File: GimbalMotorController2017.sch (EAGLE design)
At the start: 123 parts, among them J3 APP_2POS_CONFIG5V_HORIZ, Q7 MOSFET-PCHANNEL, Q8 MOSFET-PCHANNEL, Q9 MOSFET-NCHANNELAO3404A, U1 NUP4201MR6, U2 MAX3232D, U3 CSD18533Q5A, U4 CSD18533Q5A, U5 CSD18533Q5A, U6 CSD18533Q5A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

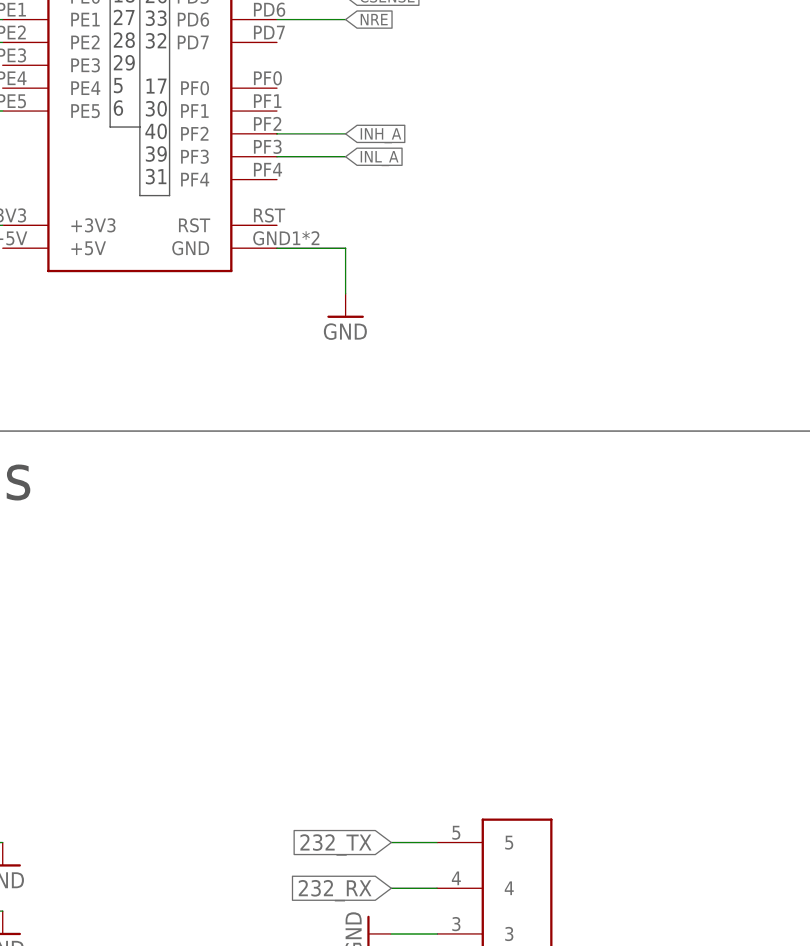
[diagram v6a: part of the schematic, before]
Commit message: Add pwm connector to external connections
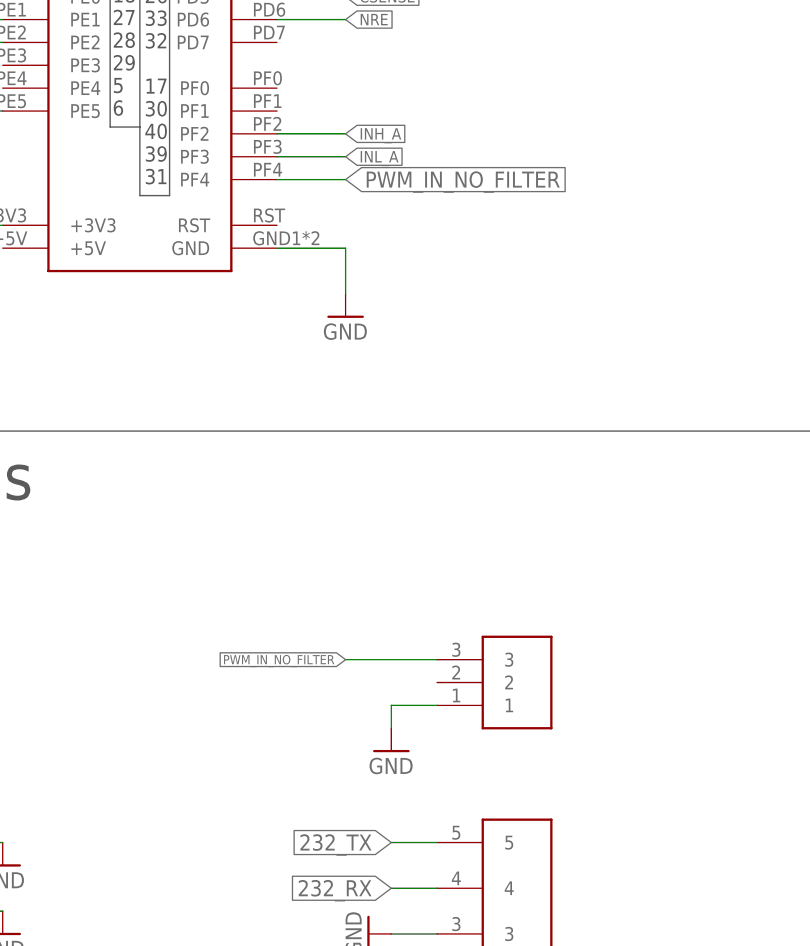
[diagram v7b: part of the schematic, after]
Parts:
- added J1: SL03THROUGH_HOLE, MRDT-Connectors:SL03THROUGH_HOLE
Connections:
- new net PWM_IN_NO_FILTER: J1.3, U$2.PF4
- net GND: now also J1.1
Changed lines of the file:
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@@
 <part name="U7" library="CSD18533" deviceset="CSD18533Q5A" device=""/>
 <part name="U8" library="CSD18533" deviceset="CSD18533Q5A" device=""/>
+<part name="J1" library="MRDT-Connectors" deviceset="SL03" device="THROUGH_HOLE"/>
+<part name="GND28" library="SparkFun-Aesthetics" deviceset="GND" device=""/>
 </parts>
 <sheets>
@@
 <instance part="U7" gate="A" x="142.24" y="12.7" rot="R90"/>
 <instance part="U8" gate="A" x="139.7" y="76.2"/>
+<instance part="J1" gate="G$1" x="325.12" y="-35.56"/>
+<instance part="GND28" gate="1" x="312.42" y="-43.18"/>
 </instances>
 <busses>
@@
 <wire x1="17.78" y1="-35.56" x2="25.4" y2="-35.56" width="0.1524" layer="91"/>
 <pinref part="GND37" gate="1" pin="GND"/>
+</segment>
+<segment>
+<pinref part="J1" gate="G$1" pin="1"/>
+<pinref part="GND28" gate="1" pin="GND"/>
+<wire x1="317.5" y1="-38.1" x2="312.42" y2="-38.1" width="0.1524" layer="91"/>
+<wire x1="312.42" y1="-38.1" x2="312.42" y2="-40.64" width="0.1524" layer="91"/>
 </segment>
 </net>
@@
 </segment>
 </net>
+<net name="PWM_IN_NO_FILTER" class="0">
+<segment>
+<pinref part="J1" gate="G$1" pin="3"/>
+<wire x1="317.5" y1="-33.02" x2="307.34" y2="-33.02" width="0.1524" layer="91"/>
+<label x="307.34" y="-33.02" size="1.016" layer="95" rot="R180" xref="yes"/>
+</segment>
+<segment>
+<pinref part="U$2" gate="G$1" pin="PF4"/>
+<wire x1="299.72" y1="20.32" x2="307.34" y2="20.32" width="0.1524" layer="91"/>
+<label x="307.34" y="20.32" size="1.778" layer="95" xref="yes"/>
+</segment>
+</net>

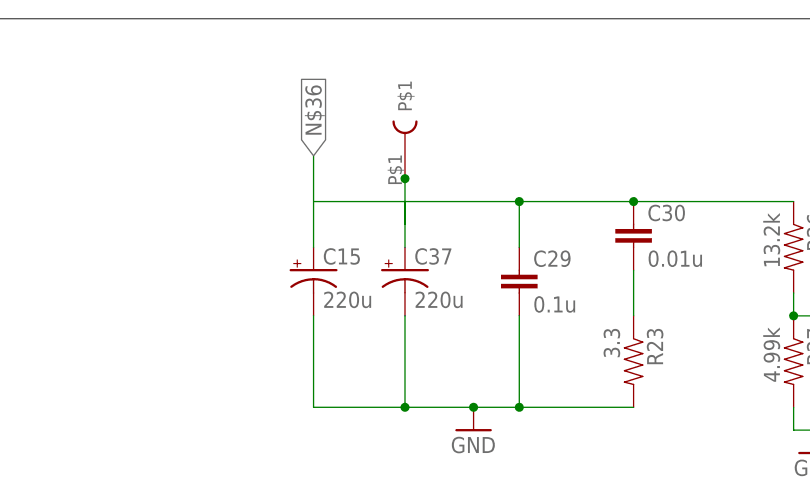
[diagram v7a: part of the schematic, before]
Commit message: Started routing traces on board
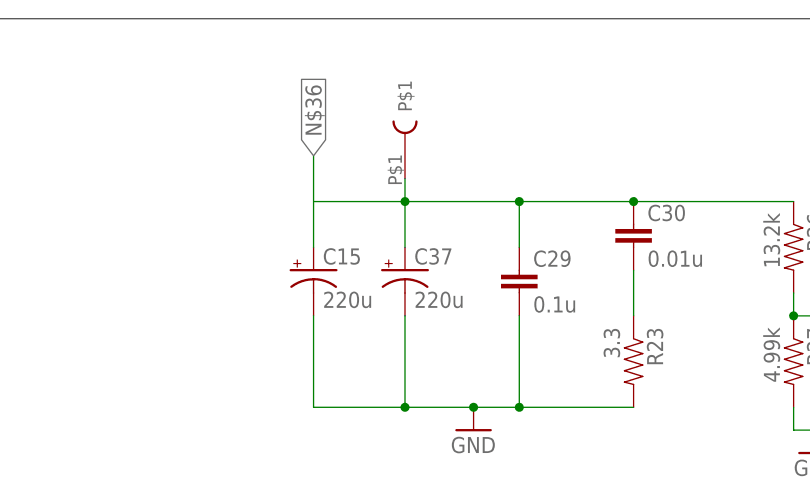
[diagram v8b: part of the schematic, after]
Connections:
- removed net N$37: U$3.P$1
- net PVDD: now also U$3.P$1
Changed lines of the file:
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@@
 <wire x1="-22.86" y1="142.24" x2="-12.7" y2="142.24" width="0.1524" layer="91"/>
 <wire x1="-12.7" y1="142.24" x2="-12.7" y2="137.16" width="0.1524" layer="91"/>
+<pinref part="U$3" gate="G$1" pin="P$1"/>
+<wire x1="-12.7" y1="142.24" x2="-12.7" y2="144.78" width="0.1524" layer="91"/>
+<junction x="-12.7" y="142.24"/>
 </segment>
 <segment>
@@
 </segment>
 </net>
-<net name="N$37" class="0">
-<segment>
-<wire x1="-12.7" y1="139.7" x2="-12.7" y2="144.78" width="0.1524" layer="91"/>
-<junction x="-12.7" y="144.78"/>
-<pinref part="U$3" gate="G$1" pin="P$1"/>
-</segment>
-</net>
